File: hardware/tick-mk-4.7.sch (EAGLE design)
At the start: 33 parts, among them IC1 TINY85-20-DIP, IC2 DS1307, IC3 L7805, IC4 MAX7219, IC5 MAX7219, J1 PROG, Y2 32.768kHz

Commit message: diddling
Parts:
- added C6: 10uF, A_butts:CAPACITOR-POLARIZEDE2-5
- added C7: 100uF, A_butts:CAPACITOR-POLARIZEDE2.5-6
- C3: value 1uF -> 0.1uF
- C4: value 10uF -> 0.1uF; device A_butts:CAPACITOR-POLARIZEDE2-5 -> A_butts:CAPACITOR-CERAMIC025-024X044
- C5: value 100uF -> 1uF; device A_butts:CAPACITOR-POLARIZEDE2.5-6 -> A_butts:CAPACITOR-CERAMIC025-024X044
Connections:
- net N$15 renamed DIG15
- net N$16 renamed DIG14
- net N$17 renamed DIG13
- net N$18 renamed DIG12
- removed net N$10: IC4.CLK
- removed net N$13: IC5.LOAD
- removed net N$14: IC5.CLK
- removed net N$19: IC5.DIG3
- removed net N$20: IC5.DIG2
- removed net N$21: IC5.DIG1
- removed net N$22: IC5.DIG0
- removed net N$23: IC4.DIG7
- removed net N$24: IC4.DIG6
- removed net N$25: IC4.DIG5
- removed net N$26: IC4.DIG4
- removed net N$27: IC4.DIG3
- removed net N$28: IC4.DIG2
- removed net N$29: IC4.DIG1
- removed net N$30: IC4.DIG0
- removed net N$31: IC4.DIN
- removed net N$32: IC5.SEGG
- removed net N$9: IC4.LOAD
- new net A1: DISPLAY1.A, DISPLAY2.A, IC4.SEGA
- new net A2: DIGIT1.A, DIGIT2.A, DIGIT3.A, DIGIT4.A, IC5.SEGA
- new net B1: DISPLAY1.B, DISPLAY2.B, IC4.SEGB
- new net B2: DIGIT1.B, DIGIT2.B, DIGIT3.B, DIGIT4.B, IC5.SEGB
- new net C1: DISPLAY1.C, DISPLAY2.C, IC4.SEGC
- new net C2: DIGIT1.C, DIGIT2.C, DIGIT3.C, DIGIT4.C, IC5.SEGC
- new net D1: DISPLAY1.D, DISPLAY2.D, IC4.SEGD
- new net D2: DIGIT1.D, DIGIT2.D, DIGIT3.D, DIGIT4.D, IC5.SEGD
- new net DIG0: DISPLAY1.DIG1, IC4.DIG0
- new net DIG1: DISPLAY1.DIG2, IC4.DIG1
- new net DIG10: DIGIT3.K1, DIGIT3.K2, IC5.DIG2
- new net DIG11: DIGIT4.K1, DIGIT4.K2, IC5.DIG3
- new net DIG2: DISPLAY1.DIG3, IC4.DIG2
- new net DIG3: DISPLAY1.DIG4, IC4.DIG3
- new net DIG4: DISPLAY2.DIG1, IC4.DIG4
- new net DIG5: DISPLAY2.DIG2, IC4.DIG5
- new net DIG6: DISPLAY2.DIG3, IC4.DIG6
- new net DIG7: DISPLAY2.DIG4, IC4.DIG7
- new net DIG8: DIGIT1.K1, DIGIT1.K2, IC5.DIG0
- new net DIG9: DIGIT2.K1, DIGIT2.K2, IC5.DIG1
- new net DP1: DISPLAY1.DP, DISPLAY2.DP, IC4.SEGDP
- new net DP2: DIGIT1.DP, DIGIT2.DP, DIGIT3.DP, DIGIT4.DP, IC5.SEGDP
- new net E1: DISPLAY1.E, DISPLAY2.E, IC4.SEGE
- new net E2: DIGIT1.E, DIGIT2.E, DIGIT3.E, DIGIT4.E, IC5.SEGE
- new net F1: DISPLAY1.F, DISPLAY2.F, IC4.SEGF
- new net F2: DIGIT1.F, DIGIT2.F, DIGIT3.F, DIGIT4.F, IC5.SEGF
- new net G1: DISPLAY1.G, DISPLAY2.G, IC4.SEGG
- new net G2: DIGIT1.G, DIGIT2.G, DIGIT3.G, DIGIT4.G, IC5.SEGG
- net CLK: now also IC4.CLK, IC5.CLK
- net DIN: now also IC4.DIN
- net GND: now also C4.2, C5.2, C6.-, C7.-, IC4.GND, IC4.GND2, IC5.GND, IC5.GND2; no longer C4.-, C5.-
- net LOAD: now also IC4.LOAD, IC5.LOAD
- net N$8: now also C6.+; no longer C4.+
- net VCC: now also C4.1, C5.1, C7.+; no longer C5.+
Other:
- moved on the sheet: DIGIT3, DIGIT4

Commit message: commit before pull
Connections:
- new net N$6: IC5.DOUT
- net A1: now also IC5.SEGA; no longer IC4.SEGA
- net A2: now also IC4.SEGA; no longer IC5.SEGA
- net B1: now also IC5.SEGB; no longer IC4.SEGB
- net B2: now also IC4.SEGB; no longer IC5.SEGB
- net C1: now also IC5.SEGC; no longer IC4.SEGC
- net C2: now also IC4.SEGC; no longer IC5.SEGC
- net D1: now also IC5.SEGD; no longer IC4.SEGD
- net D2: now also IC4.SEGD; no longer IC5.SEGD
- net DIG0: now also IC5.DIG0; no longer IC4.DIG0
- net DIG1: now also IC5.DIG1; no longer IC4.DIG1
- net DIG10: now also IC4.DIG2; no longer IC5.DIG2
- net DIG11: now also IC4.DIG3; no longer IC5.DIG3
- net DIG12: now also IC4.DIG4; no longer IC5.DIG4
- net DIG13: now also IC4.DIG5; no longer IC5.DIG5
- net DIG14: now also IC4.DIG6; no longer IC5.DIG6
- net DIG15: now also IC4.DIG7; no longer IC5.DIG7
- net DIG2: now also IC5.DIG2; no longer IC4.DIG2
- net DIG3: now also IC5.DIG3; no longer IC4.DIG3
- net DIG4: now also IC5.DIG4; no longer IC4.DIG4
- net DIG5: now also IC5.DIG5; no longer IC4.DIG5
- net DIG6: now also IC5.DIG6; no longer IC4.DIG6
- net DIG7: now also IC5.DIG7; no longer IC4.DIG7
- net DIG8: now also IC4.DIG0; no longer IC5.DIG0
- net DIG9: now also IC4.DIG1; no longer IC5.DIG1
- net DP1: now also IC5.SEGDP; no longer IC4.SEGDP
- net DP2: now also IC4.SEGDP; no longer IC5.SEGDP
- net E1: now also IC5.SEGE; no longer IC4.SEGE
- net E2: now also IC4.SEGE; no longer IC5.SEGE
- net F1: now also IC5.SEGF; no longer IC4.SEGF
- net F2: now also IC4.SEGF; no longer IC5.SEGF
- net G1: now also IC5.SEGG; no longer IC4.SEGG
- net G2: now also IC4.SEGG; no longer IC5.SEGG
- net MOSI/SDA: now also IC1.PB0(MOSI)
- net N$11: now also IC5.ISET; no longer IC4.ISET
- net N$12: now also IC4.ISET; no longer IC5.ISET
- net RST: now also IC1.RESET
- net SCK/SCL: now also IC1.PB2(SCK/ADC1)
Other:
- moved on the sheet: IC4, IC5, R4

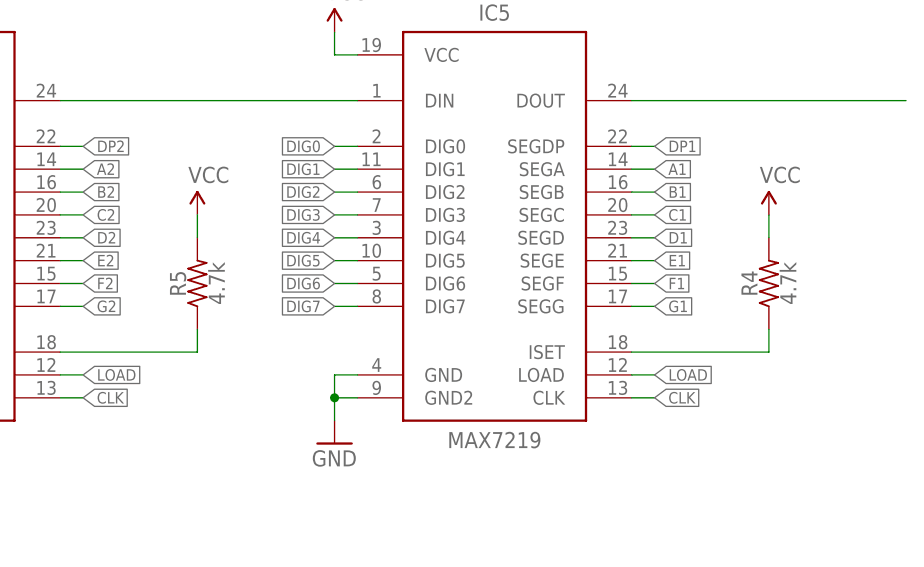
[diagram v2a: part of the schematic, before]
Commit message: more layout tinkering for the max7129 soic version. broke out into a board with only the two display drivers on it for now, will add other componets once this layout part is done.
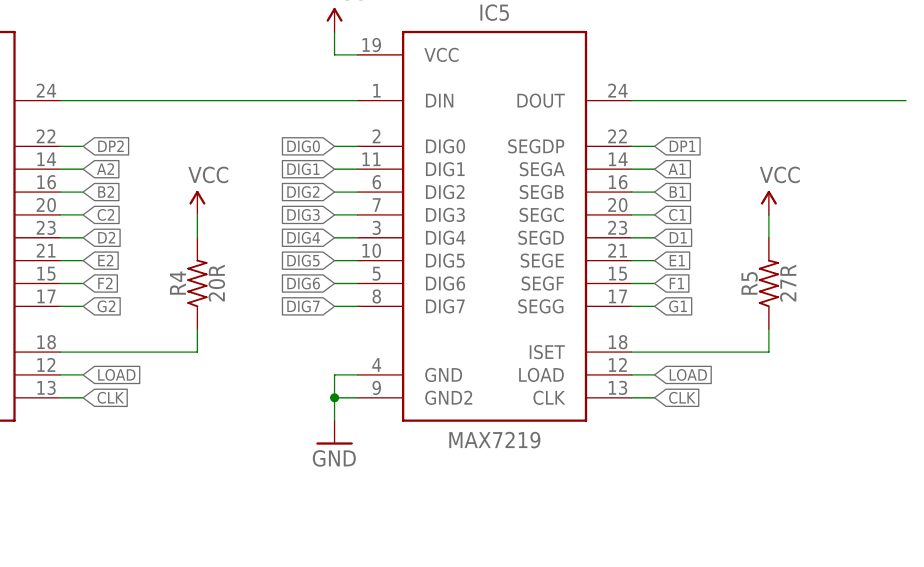
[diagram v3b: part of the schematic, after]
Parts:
- R4: value 4.7k -> 20R
- R5: value 4.7k -> 27R
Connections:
- net N$11: now also R5.1; no longer R4.1
- net N$12: now also R4.1; no longer R5.1
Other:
- moved on the sheet: R4, R5
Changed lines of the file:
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@@
 <grid distance="100" unitdist="mil" unit="mil" style="lines" multiple="1" display="yes" altdistance="2" altunitdist="mil" altunit="mil"/>
 <layers>
-<layer number="1" name="Top" color="4" fill="1" visible="no" active="no"/>
-<layer number="16" name="Bottom" color="1" fill="1" visible="no" active="no"/>
-<layer number="17" name="Pads" color="2" fill="1" visible="no" active="no"/>
-<layer number="18" name="Vias" color="2" fill="1" visible="no" active="no"/>
-<layer number="19" name="Unrouted" color="6" fill="1" visible="no" active="no"/>
-<layer number="20" name="Dimension" color="15" fill="1" visible="no" active="no"/>
-<layer number="21" name="tPlace" color="7" fill="1" visible="no" active="no"/>
-<layer number="22" name="bPlace" color="7" fill="1" visible="no" active="no"/>
-<layer number="23" name="tOrigins" color="15" fill="1" visible="no" active="no"/>
-<layer number="24" name="bOrigins" color="15" fill="1" visible="no" active="no"/>
-<layer number="25" name="tNames" color="7" fill="1" visible="no" active="no"/>
-<layer number="26" name="bNames" color="7" fill="1" visible="no" active="no"/>
-<layer number="27" name="tValues" color="7" fill="1" visible="no" active="no"/>
-<layer number="28" name="bValues" color="7" fill="1" visible="no" active="no"/>
+<layer number="1" name="Top" color="4" fill="1" visible="yes" active="no"/>
+<layer number="16" name="Bottom" color="1" fill="1" visible="yes" active="no"/>
+<layer number="17" name="Pads" color="2" fill="1" visible="yes" active="no"/>
+<layer number="18" name="Vias" color="2" fill="1" visible="yes" active="no"/>
+<layer number="19" name="Unrouted" color="6" fill="1" visible="yes" active="no"/>
+<layer number="20" name="Dimension" color="15" fill="1" visible="yes" active="no"/>
+<layer number="21" name="tPlace" color="7" fill="1" visible="yes" active="no"/>
+<layer number="22" name="bPlace" color="7" fill="1" visible="yes" active="no"/>
+<layer number="23" name="tOrigins" color="15" fill="1" visible="yes" active="no"/>
+<layer number="24" name="bOrigins" color="15" fill="1" visible="yes" active="no"/>
+<layer number="25" name="tNames" color="7" fill="1" visible="yes" active="no"/>
+<layer number="26" name="bNames" color="7" fill="1" visible="yes" active="no"/>
+<layer number="27" name="tValues" color="7" fill="1" visible="yes" active="no"/>
+<layer number="28" name="bValues" color="7" fill="1" visible="yes" active="no"/>
 <layer number="29" name="tStop" color="7" fill="3" visible="no" active="no"/>
 <layer number="30" name="bStop" color="7" fill="6" visible="no" active="no"/>
@@
 <layer number="35" name="tGlue" color="7" fill="4" visible="no" active="no"/>
 <layer number="36" name="bGlue" color="7" fill="5" visible="no" active="no"/>
-<layer number="37" name="tTest" color="7" fill="1" visible="no" active="no"/>
-<layer number="38" name="bTest" color="7" fill="1" visible="no" active="no"/>
+<layer number="37" name="tTest" color="7" fill="1" visible="yes" active="no"/>
+<layer number="38" name="bTest" color="7" fill="1" visible="yes" active="no"/>
 <layer number="39" name="tKeepout" color="4" fill="11" visible="no" active="no"/>
 <layer number="40" name="bKeepout" color="1" fill="11" visible="no" active="no"/>
@@
 <layer number="44" name="Drills" color="7" fill="1" visible="no" active="no"/>
 <layer number="45" name="Holes" color="7" fill="1" visible="no" active="no"/>
-<layer number="46" name="Milling" color="3" fill="1" visible="no" active="no"/>
-<layer number="47" name="Measures" color="5" fill="1" visible="no" active="no"/>
-<layer number="48" name="Document" color="7" fill="1" visible="no" active="no"/>
-<layer number="49" name="Reference" color="7" fill="1" visible="no" active="no"/>
-<layer number="50" name="dxf" color="7" fill="1" visible="no" active="no"/>
-<layer number="51" name="tDocu" color="7" fill="1" visible="no" active="no"/>
-<layer number="52" name="bDocu" color="7" fill="1" visible="no" active="no"/>
-<layer number="53" name="tGND_GNDA" color="7" fill="9" visible="no" active="no"/>
-<layer number="54" name="bGND_GNDA" color="1" fill="9" visible="no" active="no"/>
-<layer number="56" name="wert" color="7" fill="1" visible="no" active="no"/>
-<layer number="57" name="tCAD" color="7" fill="1" visible="no" active="no"/>
+<layer number="46" name="Milling" color="3" fill="1" visible="yes" active="no"/>
+<layer number="47" name="Measures" color="5" fill="1" visible="yes" active="no"/>
+<layer number="48" name="Document" color="7" fill="1" visible="yes" active="no"/>
+<layer number="49" name="Reference" color="7" fill="1" visible="yes" active="no"/>
+<layer number="50" name="dxf" color="7" fill="1" visible="yes" active="no"/>
+<layer number="51" name="tDocu" color="7" fill="1" visible="yes" active="no"/>
+<layer number="52" name="bDocu" color="7" fill="1" visible="yes" active="no"/>
+<layer number="53" name="tGND_GNDA" color="7" fill="9" visible="yes" active="no"/>
+<layer number="54" name="bGND_GNDA" color="1" fill="9" visible="yes" active="no"/>
+<layer number="56" name="wert" color="7" fill="1" visible="yes" active="no"/>
+<layer number="57" name="tCAD" color="7" fill="1" visible="yes" active="no"/>
 <layer number="91" name="Nets" color="2" fill="1" visible="yes" active="yes"/>
 <layer number="92" name="Busses" color="1" fill="1" visible="yes" active="yes"/>
@@
 <part name="SUPPLY11" library="A_butts" deviceset="VCC" device=""/>
 <part name="SUPPLY13" library="A_butts" deviceset="VCC" device=""/>
-<part name="R5" library="A_butts" deviceset="RESISTOR" device="PTH-AXIAL-7.62MM" value="4.7k"/>
+<part name="R4" library="A_butts" deviceset="RESISTOR" device="PTH-AXIAL-7.62MM" value="20R"/>
 <part name="GND4" library="A_butts" deviceset="GND" device=""/>
 <part name="GND6" library="A_butts" deviceset="GND" device=""/>
@@
 <part name="SUPPLY2" library="A_butts" deviceset="VCC" device=""/>
 <part name="SUPPLY12" library="A_butts" deviceset="VCC" device=""/>
-<part name="R4" library="A_butts" deviceset="RESISTOR" device="PTH-AXIAL-7.62MM" value="4.7k"/>
+<part name="R5" library="A_butts" deviceset="RESISTOR" device="PTH-AXIAL-7.62MM" value="27R"/>
 <part name="GND3" library="A_butts" deviceset="GND" device=""/>
 </parts>
@@
 <instance part="SUPPLY11" gate="G$1" x="304.8" y="101.6"/>
 <instance part="SUPPLY13" gate="G$1" x="353.06" y="81.28"/>
-<instance part="R5" gate="G$1" x="353.06" y="73.66" rot="R90"/>
+<instance part="R4" gate="G$1" x="353.06" y="73.66" rot="R90"/>
 <instance part="GND4" gate="1" x="304.8" y="55.88"/>
 <instance part="GND6" gate="1" x="195.58" y="93.98"/>
@@
 <instance part="SUPPLY2" gate="G$1" x="368.3" y="101.6"/>
 <instance part="SUPPLY12" gate="G$1" x="416.56" y="81.28"/>
-<instance part="R4" gate="G$1" x="416.56" y="73.66" rot="R90"/>
+<instance part="R5" gate="G$1" x="416.56" y="73.66" rot="R90"/>
 <instance part="GND3" gate="1" x="368.3" y="55.88"/>
 </instances>
@@
 </segment>
 <segment>
-<pinref part="R5" gate="G$1" pin="2"/>
+<pinref part="R4" gate="G$1" pin="2"/>
 <pinref part="SUPPLY13" gate="G$1" pin="VCC"/>
 <wire x1="353.06" y1="78.74" x2="353.06" y2="81.28" width="0.1524" layer="91"/>
@@
 </segment>
 <segment>
-<pinref part="R4" gate="G$1" pin="2"/>
+<pinref part="R5" gate="G$1" pin="2"/>
 <pinref part="SUPPLY12" gate="G$1" pin="VCC"/>
 <wire x1="416.56" y1="78.74" x2="416.56" y2="81.28" width="0.1524" layer="91"/>
@@
 <segment>
 <pinref part="IC4" gate="G$1" pin="ISET"/>
-<pinref part="R5" gate="G$1" pin="1"/>
+<pinref part="R4" gate="G$1" pin="1"/>
 <wire x1="353.06" y1="68.58" x2="353.06" y2="66.04" width="0.1524" layer="91"/>
 <wire x1="353.06" y1="66.04" x2="337.82" y2="66.04" width="0.1524" layer="91"/>
@@
 <segment>
 <pinref part="IC5" gate="G$1" pin="ISET"/>
-<pinref part="R4" gate="G$1" pin="1"/>
+<pinref part="R5" gate="G$1" pin="1"/>
 <wire x1="416.56" y1="68.58" x2="416.56" y2="66.04" width="0.1524" layer="91"/>
 <wire x1="416.56" y1="66.04" x2="401.32" y2="66.04" width="0.1524" layer="91"/>
